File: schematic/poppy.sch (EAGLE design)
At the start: 18 parts, among them Q1 8MHz

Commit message: routed everything
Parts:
- removed U$1: ATMEGA16U4TQFP44, p1poppy:ATMEGA16U4TQFP44
- removed U$2: MBI5030GFSOP-24, p1poppy:MBI5030GFSOP-24
- added U1: ATMEGA16U4TQFP44, p1poppy:ATMEGA16U4TQFP44
- added U2: MBI5030GFSOP-24, p1poppy:MBI5030GFSOP-24
- R1: value 10k -> 22; device resistor:R-EU_R3216 -> resistor:R-EU_R1206
- R2: value 1k -> 22; device resistor:R-EU_R3216 -> resistor:R-EU_R1206
- R3: value 1k -> 10k; device resistor:R-EU_R3216 -> resistor:R-EU_R1206
- R4, R5: value 22 -> 1k; device resistor:R-EU_R3216 -> resistor:R-EU_R1206
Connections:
- new net DCLK: U1.PB4, U2.DCLK
- new net SDI: U1.PB5, U2.SDI
- net CLK0: now also U1.PC7, U2.GCLK; no longer U$1.PC7, U$2.GCLK
- net D+: now also R1.2; no longer R4.2
- net D-: now also R2.2; no longer R5.2
- net GND: now also LED1.C, R5.1, U1.AREF, U1.GND15, U1.GND23, U1.GND35, U1.GND43, U1.UGND, U2.GND; no longer R2.1, R3.1, U$1.AREF, U$1.GND15, U$1.GND23, U$1.GND35, U$1.GND43, U$1.UGND, U$2.GND
- net LATCH: now also U1.PB6, U2.LE; no longer U$1.PB0, U$2.LE
- net MISO: now also U1.PB3; no longer U$1.PB3
- net MOSI/DATA: now also U1.PB2; no longer U$1.PB2, U$2.SDI
- net N$1: now also R4.2, U1.PF6; no longer LED1.A, U$1.PF6
- net N$10: now also R2.1, U1.D-; no longer R5.1, U$1.D-
- net N$2: now also R5.2, U2.R-EXT; no longer R3.2, U$2.R-EXT
- net N$3: now also U2./OUT0; no longer U$2./OUT0
- net N$4: now also U1.UCAP; no longer U$1.UCAP
- net N$5: now also U2./OUT1; no longer U$2./OUT1
- net N$6: now also U2./OUT2; no longer U$2./OUT2
- net N$7: now also LED1.A, R4.1; no longer LED1.C, R2.2
- net N$9: now also R1.1, U1.D+; no longer R4.1, U$1.D+
- net RESET: now also R3.1, U1.RESET; no longer R1.1, U$1.RESET
- net SCK: now also U1.PB1; no longer U$1.PB1, U$2.DCLK
- net VCC: now also R3.2, U1.AVCC24, U1.AVCC44, U1.UVCC, U1.VBUS, U1.VCC14, U1.VCC34, U2.VDD; no longer R1.2, U$1.AVCC24, U$1.AVCC44, U$1.UVCC, U$1.VBUS, U$1.VCC14, U$1.VCC34, U$2.VDD
- net XTAL1: now also U1.XTAL1; no longer U$1.XTAL1
- net XTAL2: now also U1.XTAL2; no longer U$1.XTAL2
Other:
- moved on the sheet: C1, C2, C3, C4, C5, C6, ISP, LED1, LED2, Q1, R1, R2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

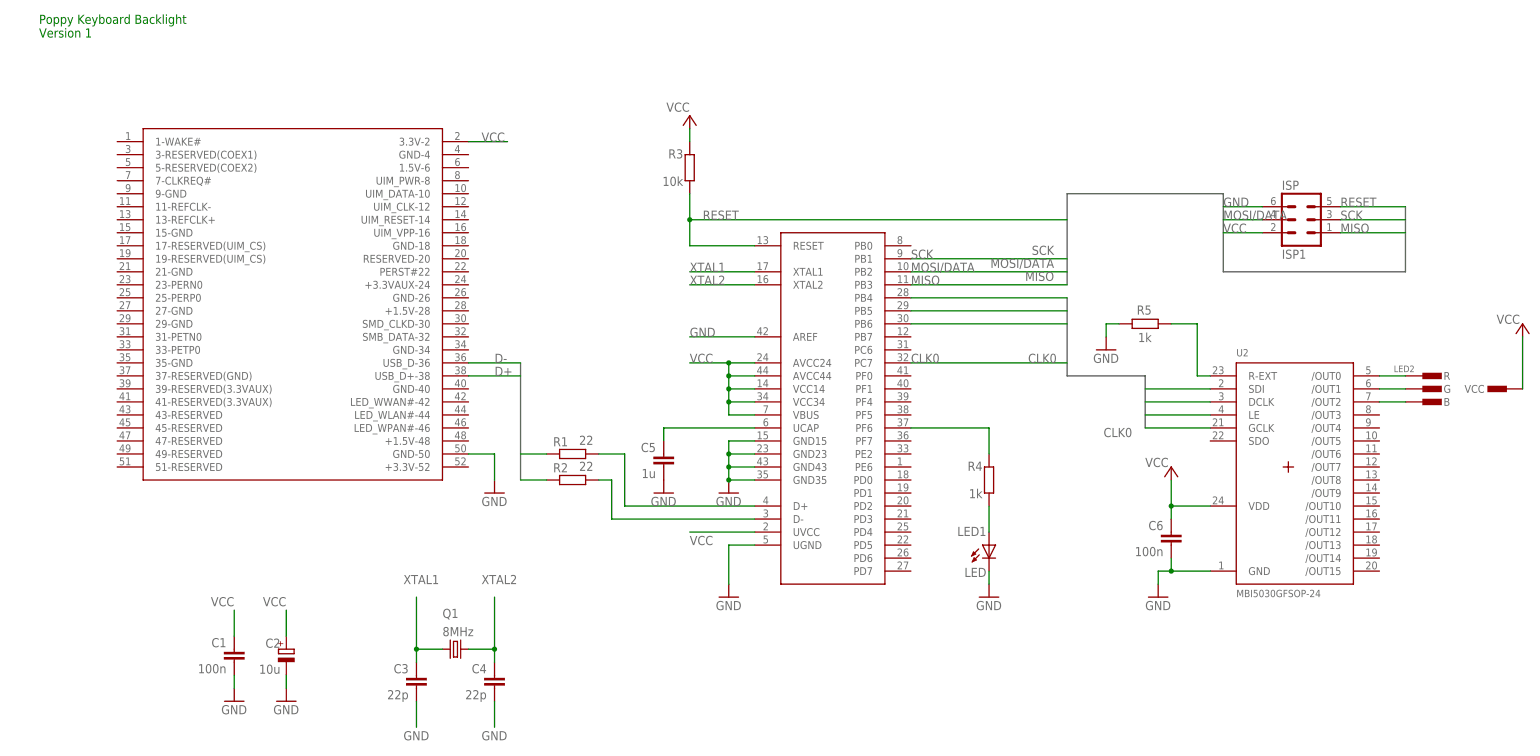
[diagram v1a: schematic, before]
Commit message: added miniusb and second led
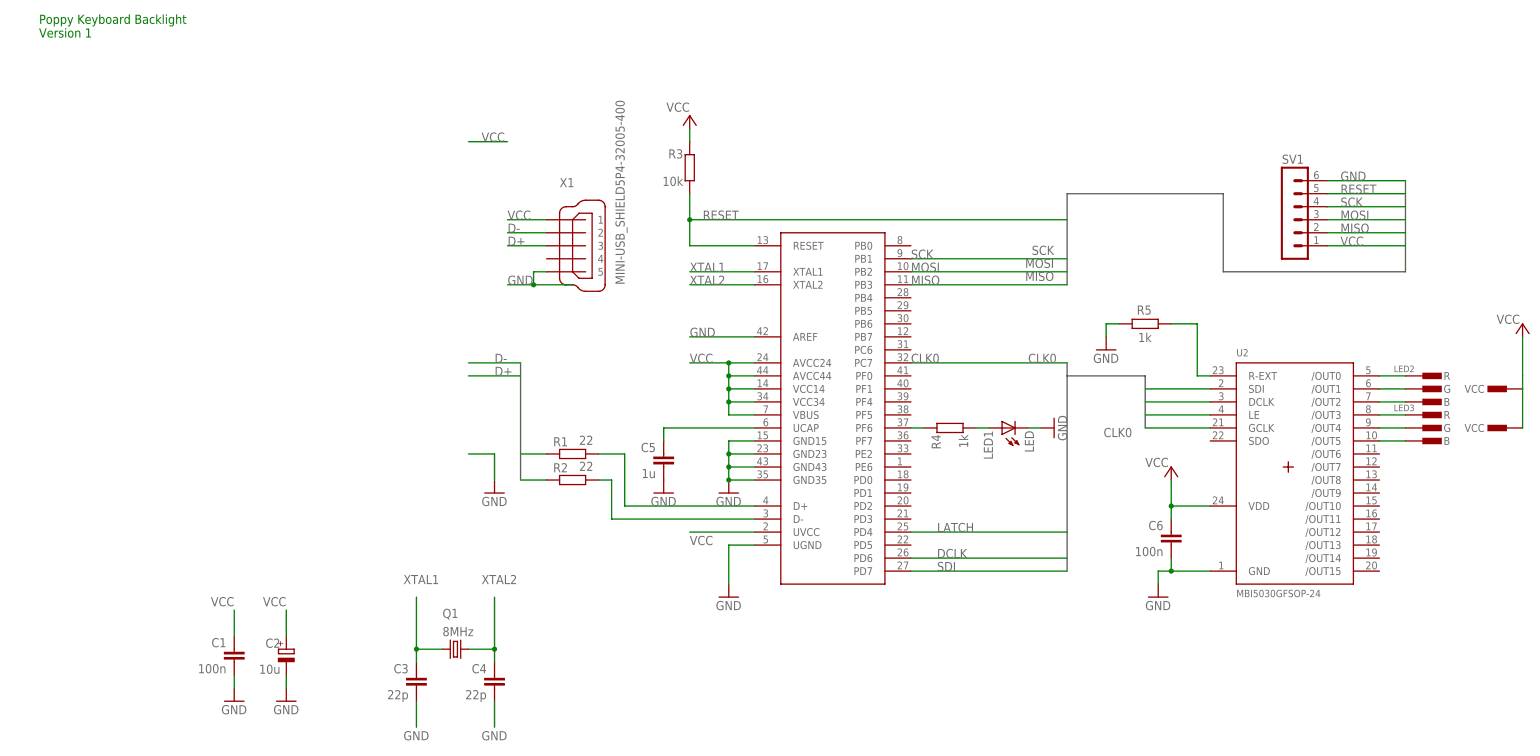
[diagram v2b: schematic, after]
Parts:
- removed EDGE: FULL-MINI-PCI-E, mini-pci-e:FULL-MINI-PCI-E
- removed ISP: ISP1, con-lstb:MA03-2
- added LED3: CON-RGB-LED-EXT, _led-rgb:CON-RGB-LED-EXT
- added SV1: (no value), con-lstb:MA06-1
- added X1: MINI-USB_SHIELD5P4-32005-400, con-cypressindustries:MINI-USB_SHIELD5P4-32005-400
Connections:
- removed net MOSI/DATA: ISP.4, U1.PB2
- new net MOSI: SV1.3, U1.PB2
- new net N$11: LED3.R, U2./OUT3
- new net N$12: LED3.G, U2./OUT4
- new net N$13: LED3.B, U2./OUT5
- net D+: now also X1G$1.3; no longer EDGEG$1.USB_D+-38
- net D-: now also X1G$1.2; no longer EDGEG$1.USB_D-36
- net DCLK: now also U1.PD6; no longer U1.PB4
- net GND: now also SV1.6, X1G$1.5; no longer EDGEG$1.GND-50, ISP.6
- net LATCH: now also U1.PD4; no longer U1.PB6
- net MISO: now also SV1.2; no longer ISP.1
- net RESET: now also SV1.5; no longer ISP.5
- net SCK: now also SV1.4; no longer ISP.3
- net SDI: now also U1.PD7; no longer U1.PB5
- net VCC: now also LED3.VCC, SV1.1, X1G$1.1; no longer EDGEG$1.3.3V-2, ISP.2
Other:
- moved on the sheet: LED1, R4
